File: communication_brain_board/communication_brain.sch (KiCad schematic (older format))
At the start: 39 parts, among them IC1 TM1637, J1 UART, J2 Batt, J3 RS485, J4 CAN, SW1 Reset, SW2 Programm, U1 LM2596T-ADJ, U2 L78L33_TO92, U3 ESP-12E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

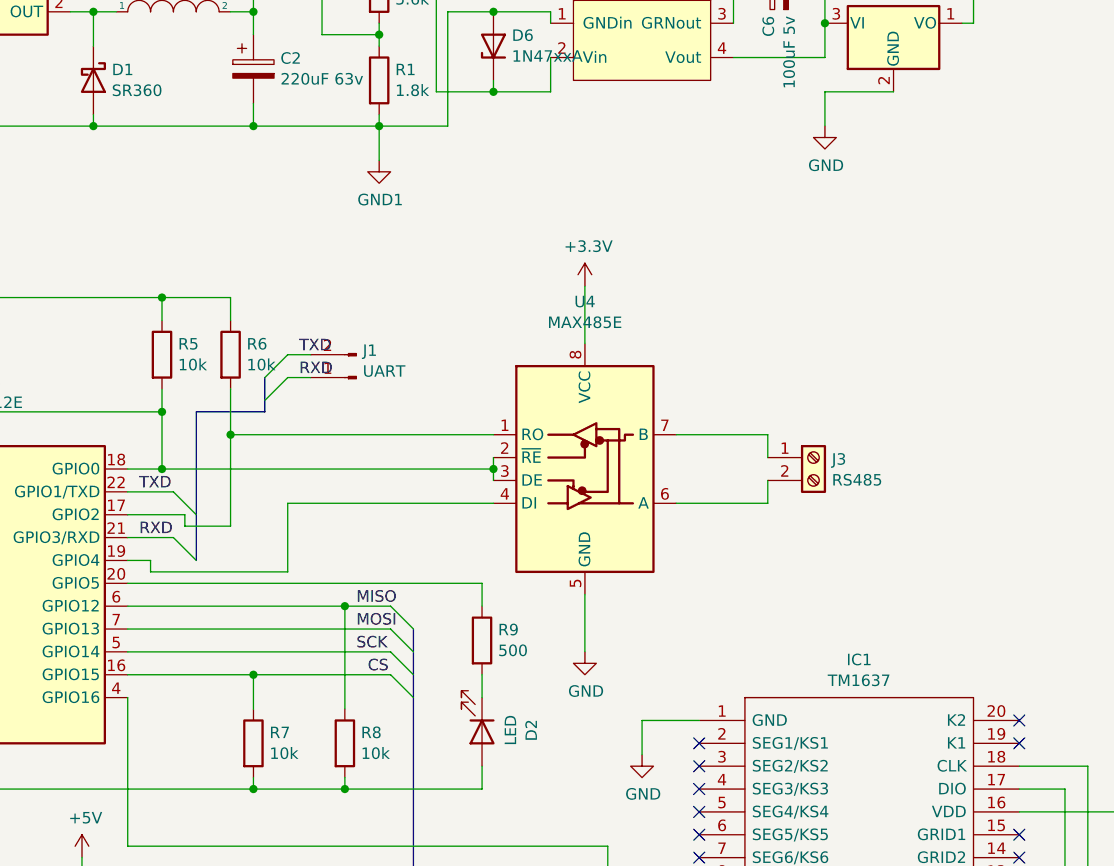
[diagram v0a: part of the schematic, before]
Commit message: added:  - tcp modbus communication to battery  - udb proadcast of battery stait  - prepare for RS485 communication with invertor  - updated readmy (modules needed for build)  - stability
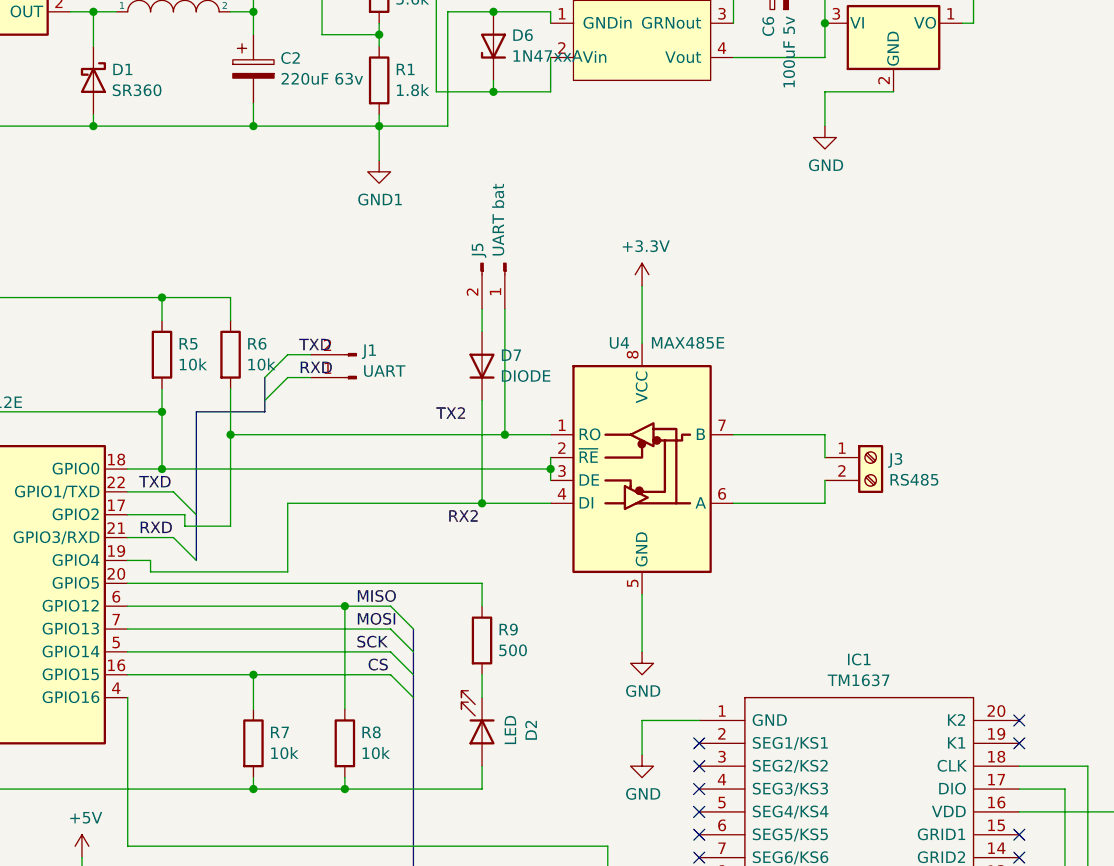
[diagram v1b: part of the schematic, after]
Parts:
- added D7: DIODE, symbol Simulation_SPICE:DIODE
- added J5: UART bat, Connector_PinHeader_2.00mm:PinHeader_1x02_P2.00mm_Vertical, symbol Connector:Conn_01x02_Male
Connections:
- net at R6.2, U3.17 (GPIO2), U4.1 (RO): now also J5.1 (Pin_1)
- net at U3.19 (GPIO4), U4.4 (DI): now also D7.2 (K)
- new net: D7.1 (A), J5.2 (Pin_2)
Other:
- moved on the sheet: J3, U4
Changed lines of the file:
@@
 L Interface_UART:MAX485E U4
 U 1 1 600D8FD6
-P 6400 3750
-F 0 "U4" H 6400 4431 50  0000 C CNN
-F 1 "MAX485E" H 6400 4340 50  0000 C CNN
-F 2 "Package_SO:SOIC-8_5.23x5.23mm_P1.27mm" H 6400 3050 50  0001 C CNN
-F 3 "https://datasheets.maximintegrated.com/en/ds/MAX1487E-MAX491E.pdf" H 6400 3800 50  0001 C CNN
-	1    6400 3750
-	1    0    0    -1
-$EndComp
-Wire Wire Line
-	6000 3750 6000 3800
-Connection ~ 6000 3800
-Wire Wire Line
-	6000 3800 6000 3850
-Wire Wire Line
-	5100 3950 6000 3950
+P 6650 3750
+F 0 "U4" H 6550 4250 50  0000 C CNN
+F 1 "MAX485E" H 6850 4250 50  0000 C CNN
+F 2 "Package_SO:SOIC-8_5.23x5.23mm_P1.27mm" H 6650 3050 50  0001 C CNN
+F 3 "https://datasheets.maximintegrated.com/en/ds/MAX1487E-MAX491E.pdf" H 6650 3800 50  0001 C CNN
+	1    6650 3750
+	1    0    0    -1
+$EndComp
 $Comp
 L Device:R R8
@@
 L power:GND #PWR0109
 U 1 1 600F22C2
-P 6400 4600
-F 0 "#PWR0109" H 6400 4350 50  0001 C CNN
-F 1 "GND" H 6405 4427 50  0000 C CNN
-F 2 "" H 6400 4600 50  0001 C CNN
-F 3 "" H 6400 4600 50  0001 C CNN
-	1    6400 4600
+P 6650 4600
+F 0 "#PWR0109" H 6650 4350 50  0001 C CNN
+F 1 "GND" H 6655 4427 50  0000 C CNN
+F 2 "" H 6650 4600 50  0001 C CNN
+F 3 "" H 6650 4600 50  0001 C CNN
+	1    6650 4600
 	1    0    0    -1
 $EndComp
@@
 L Connector:Screw_Terminal_01x02 J3
 U 1 1 60052B8F
-P 7400 3750
-F 0 "J3" H 7480 3742 50  0000 L CNN
-F 1 "RS485" H 7480 3651 50  0000 L CNN
-F 2 "TerminalBlock_4Ucon:TerminalBlock_4Ucon_1x02_P3.50mm_Horizontal" H 7400 3750 50  0001 C CNN
-F 3 "~" H 7400 3750 50  0001 C CNN
-	1    7400 3750
+P 7650 3750
+F 0 "J3" H 7730 3742 50  0000 L CNN
+F 1 "RS485" H 7730 3651 50  0000 L CNN
+F 2 "TerminalBlock_4Ucon:TerminalBlock_4Ucon_1x02_P3.50mm_Horizontal" H 7650 3750 50  0001 C CNN
+F 3 "~" H 7650 3750 50  0001 C CNN
+	1    7650 3750
 	1    0    0    -1
 $EndComp
@@
 	1600 1500 1600 2300
 Wire Wire Line
-	7200 3750 7200 3650
-Wire Wire Line
-	7200 3650 6800 3650
-Wire Wire Line
-	7200 3850 7200 3950
-Wire Wire Line
-	7200 3950 6800 3950
+	7450 3750 7450 3650
+Wire Wire Line
+	7450 3650 7050 3650
+Wire Wire Line
+	7450 3850 7450 3950
+Wire Wire Line
+	7450 3950 7050 3950
 $Comp
 L power:+3.3V #PWR0110
@@
 	2100 1350 2100 1500
 Wire Wire Line
-	4850 3650 6000 3650
-Connection ~ 4550 3800
-Wire Wire Line
 	4650 4000 4650 4050
 Wire Wire Line
@@
 Wire Wire Line
 	5100 3950 5100 4250
-Wire Wire Line
-	4550 3800 6000 3800
 $Comp
 L power:+3.3V #PWR0108
 U 1 1 600EF5EB
-P 6400 3000
-F 0 "#PWR0108" H 6400 2850 50  0001 C CNN
-F 1 "+3.3V" H 6415 3173 50  0000 C CNN
-F 2 "" H 6400 3000 50  0001 C CNN
-F 3 "" H 6400 3000 50  0001 C CNN
-	1    6400 3000
-	1    0    0    -1
-$EndComp
-Wire Wire Line
-	6400 3250 6400 3000
-Wire Wire Line
-	6400 4350 6400 4600
+P 6650 3000
+F 0 "#PWR0108" H 6650 2850 50  0001 C CNN
+F 1 "+3.3V" H 6665 3173 50  0000 C CNN
+F 2 "" H 6650 3000 50  0001 C CNN
+F 3 "" H 6650 3000 50  0001 C CNN
+	1    6650 3000
+	1    0    0    -1
+$EndComp
+Wire Wire Line
+	6650 3250 6650 3000
+Wire Wire Line
+	6650 4350 6650 4600
 $Comp
 L Device:LED D2
@@
 Wire Wire Line
 	6600 5650 6600 6150
+Wire Wire Line
+	6250 3800 6250 3850
+Connection ~ 6250 3800
+Wire Wire Line
+	6250 3750 6250 3800
+Wire Wire Line
+	4550 3800 6250 3800
+Connection ~ 4550 3800
+Wire Wire Line
+	4850 3650 6050 3650
+Wire Wire Line
+	5100 3950 5950 3950
+$Comp
+L Connector:Conn_01x02_Male J5
+U 1 1 61AAB19B
+P 6050 2900
+F 0 "J5" H 6022 2782 50  0000 R CNN
+F 1 "UART bat" H 6022 2873 50  0000 R CNN
+F 2 "Connector_PinHeader_2.00mm:PinHeader_1x02_P2.00mm_Vertical" H 6050 2900 50  0001 C CNN
+F 3 "~" H 6050 2900 50  0001 C CNN
+	1    6050 2900
+	0    1    1    0
+$EndComp
+Connection ~ 6050 3650
+Wire Wire Line
+	6050 3650 6250 3650
+Wire Wire Line
+	5950 3500 5950 3950
+Connection ~ 5950 3950
+Wire Wire Line
+	5950 3950 6250 3950
+Text Label 5800 4050 0    50   ~ 0
+RX2
+Text Label 5750 3600 0    50   ~ 0
+TX2
+$Comp
+L Simulation_SPICE:DIODE D7
+U 1 1 61B2C4B9
+P 5950 3350
+F 0 "D7" V 5904 3430 50  0000 L CNN
+F 1 "DIODE" V 5995 3430 50  0000 L CNN
+F 2 "" H 5950 3350 50  0001 C CNN
+F 3 "~" H 5950 3350 50  0001 C CNN
+F 4 "Y" H 5950 3350 50  0001 L CNN "Spice_Netlist_Enabled"
+F 5 "D" H 5950 3350 50  0001 L CNN "Spice_Primitive"
+	1    5950 3350
+	0    1    1    0
+$EndComp
+Wire Wire Line
+	6050 3100 6050 3650
+Wire Wire Line
+	5950 3200 5950 3100
 Wire Bus Line
 	4700 3550 4700 4200
